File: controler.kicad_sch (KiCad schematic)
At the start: 37 parts, among them J1 USB_BOOT, J12 Conn_01x04_Pin, J2 Conn_ARM_JTAG_SWD_10, SW1 SW_DIP_x08, U1 NCP1117-3.3_SOT223, U1 RP2040, U2 W25Q128JVS, Y1 Crystal

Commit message: ECR fixes
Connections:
- net SWCLK is gone; now on net SWDCLK: U1.24 (SWCLK)
- net GND: no longer U1.28 (GPIO17)
- no-connect marks 2 -> 3
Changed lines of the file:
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@@
   (no_connect (at 185.42 138.43))
   (no_connect (at 185.42 135.89))
+  (no_connect (at 130.81 95.25))
   (wire (pts (xy 222.25 30.48) (xy 209.55 30.48))
     (stroke (width 0) (type default))
@@
     (stroke (width 0) (type default))
   )
-  (wire (pts (xy 144.78 95.25) (xy 130.81 95.25))
-    (stroke (width 0) (type default))
-  )
   (wire (pts (xy 102.87 44.45) (xy 102.87 41.91))
-    (stroke (width 0) (type default))
-  )
-  (wire (pts (xy 144.78 97.79) (xy 144.78 95.25))
     (stroke (width 0) (type default))
   )
@@
     (effects (font (size 1.27 1.27)) (justify left bottom))
   )
-  (label "SWCLK" (at 77.47 118.11 180) (fields_autoplaced)
+  (label "SWDCLK" (at 77.47 118.11 180) (fields_autoplaced)
     (effects (font (size 1.27 1.27)) (justify right bottom))
   )
@@
     (effects (font (size 1.27 1.27)) (justify left))
   )
-  (hierarchical_label "3V3" (shape output) (at 90.17 162.56 0) (fields_autoplaced)
+  (hierarchical_label "+3V3" (shape output) (at 90.17 162.56 0) (fields_autoplaced)
     (effects (font (size 1.27 1.27)) (justify left))
   )
@@
         )
       )
-    )
-  )
-  (symbol (lib_id "power:GND") (at 144.78 97.79 0) (unit 1)
-    (in_bom yes) (on_board yes) (dnp no) (fields_autoplaced)
-    (property "Reference" "#PWR049" (at 144.78 104.14 0)
-      (effects (font (size 1.27 1.27)) hide)
-    )
-    (property "Value" "GND" (at 144.78 102.87 0)
-      (effects (font (size 1.27 1.27)))
-    )
-    (property "Footprint" "" (at 144.78 97.79 0)
-      (effects (font (size 1.27 1.27)) hide)
-    )
-    (property "Datasheet" "" (at 144.78 97.79 0)
-      (effects (font (size 1.27 1.27)) hide)
-    )
-    (pin "1")
-    (instances
-      (project "SmartishFairy"
-        (path "/c494d399-9c3e-4fb0-8fd0-96c74769e433/c3e5f29d-a8aa-4f99-a65b-6663a6477720"
-          (reference "#PWR049") (unit 1)
-        )
-      )

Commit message: More ECR fixes
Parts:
- added R30: 1K, symbol Device:R
- R24, R25, R26, R27: value R -> 1K
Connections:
- net GND: now also R30.2
- net at U1.28 (GPIO17): now also R30.1
- no-connect marks 3 -> 2
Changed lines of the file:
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@@
   (no_connect (at 185.42 138.43))
   (no_connect (at 185.42 135.89))
-  (no_connect (at 130.81 95.25))
   (wire (pts (xy 222.25 30.48) (xy 209.55 30.48))
     (stroke (width 0) (type default))
@@
     (stroke (width 0) (type default))
   )
+  (wire (pts (xy 130.81 95.25) (xy 139.7 95.25))
+    (stroke (width 0) (type default))
+  )
   (wire (pts (xy 130.81 62.23) (xy 133.35 62.23))
     (stroke (width 0) (type default))
@@
     (stroke (width 0) (type default))
   )
+  (wire (pts (xy 156.21 97.79) (xy 156.21 95.25))
+    (stroke (width 0) (type default))
+  )
   (wire (pts (xy 34.29 162.56) (xy 49.53 162.56))
     (stroke (width 0) (type default))
@@
   )
   (wire (pts (xy 62.23 97.79) (xy 62.23 99.06))
+    (stroke (width 0) (type default))
+  )
+  (wire (pts (xy 147.32 95.25) (xy 156.21 95.25))
     (stroke (width 0) (type default))
   )
@@
     )
   )
+  (symbol (lib_id "Device:R") (at 143.51 95.25 90) (unit 1)
+    (in_bom yes) (on_board yes) (dnp no) (fields_autoplaced)
+    (property "Reference" "R30" (at 143.51 90.17 90)
+      (effects (font (size 1.27 1.27)))
+    )
+    (property "Value" "1K" (at 143.51 92.71 90)
+      (effects (font (size 1.27 1.27)))
+    )
+    (property "Footprint" "" (at 143.51 97.028 90)
+      (effects (font (size 1.27 1.27)) hide)
+    )
+    (property "Datasheet" "~" (at 143.51 95.25 0)
+      (effects (font (size 1.27 1.27)) hide)
+    )
+    (pin "1")
+    (pin "2")
+    (instances
+      (project "SmartishFairy"
+        (path "/c494d399-9c3e-4fb0-8fd0-96c74769e433/c3e5f29d-a8aa-4f99-a65b-6663a6477720"
+          (reference "R30") (unit 1)
+        )
+      )
+    )
+  )
   (symbol (lib_id "power:GND") (at 172.72 153.67 0) (unit 1)
     (in_bom yes) (on_board yes) (dnp no)
@@
       (effects (font (size 1.27 1.27)) (justify left))
     )
-    (property "Value" "R" (at 179.07 75.565 0)
+    (property "Value" "1K" (at 179.07 75.565 0)
       (effects (font (size 1.27 1.27)) (justify left))
     )
@@
         (path "/c494d399-9c3e-4fb0-8fd0-96c74769e433/c3e5f29d-a8aa-4f99-a65b-6663a6477720"
           (reference "#PWR070") (unit 1)
+        )
+      )
+    )
+  )
+  (symbol (lib_id "power:GND") (at 156.21 97.79 0) (unit 1)
+    (in_bom yes) (on_board yes) (dnp no) (fields_autoplaced)
+    (property "Reference" "#PWR049" (at 156.21 104.14 0)
+      (effects (font (size 1.27 1.27)) hide)
+    )
+    (property "Value" "GND" (at 156.21 102.87 0)
+      (effects (font (size 1.27 1.27)))
+    )
+    (property "Footprint" "" (at 156.21 97.79 0)
+      (effects (font (size 1.27 1.27)) hide)
+    )
+    (property "Datasheet" "" (at 156.21 97.79 0)
+      (effects (font (size 1.27 1.27)) hide)
+    )
+    (pin "1")
+    (instances
+      (project "SmartishFairy"
+        (path "/c494d399-9c3e-4fb0-8fd0-96c74769e433/c3e5f29d-a8aa-4f99-a65b-6663a6477720"
+          (reference "#PWR049") (unit 1)
         )
       )
@@
       (effects (font (size 1.27 1.27)) (justify left))
     )
-    (property "Value" "R" (at 199.39 75.565 0)
+    (property "Value" "1K" (at 199.39 75.565 0)
       (effects (font (size 1.27 1.27)) (justify left))
     )
@@
       (effects (font (size 1.27 1.27)) (justify left))
     )
-    (property "Value" "R" (at 189.23 75.565 0)
+    (property "Value" "1K" (at 189.23 75.565 0)
       (effects (font (size 1.27 1.27)) (justify left))
     )
@@
       (effects (font (size 1.27 1.27)) (justify left))
     )
-    (property "Value" "R" (at 209.55 75.565 0)
-      (effects (font (size 1.27 1.27)) (justify left))
-    )
+    (property "Value" "1K" (at 209.55 75.565 0)
+      (effects (font (size 1.27 1.27)) (justify left))
+    )

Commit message: ECR fixes
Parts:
- C1, C4: value 10u -> 10uF
- C19, C20, C21, C22, C23, C24, C25, C26, C27, C28, C29, C30, C31, C32: footprint (none) -> Capacitor_SMD:C_0805_2012Metric
- D4, D5, D6, D7: footprint (none) -> LED_SMD:LED_0805_2012Metric
- J1: footprint (none) -> Connector_PinHeader_2.54mm:PinHeader_1x02_P2.54mm_Vertical
- J12: footprint (none) -> Connector_PinHeader_2.54mm:PinHeader_1x04_P2.54mm_Vertical
- J2: footprint (none) -> Connector_PinHeader_1.27mm:PinHeader_2x05_P1.27mm_Vertical_SMD
- R19, R20, R21, R22, R23, R24, R25, R26, R27, R30: footprint (none) -> Resistor_SMD:R_0805_2012Metric
- SW1: footprint (none) -> Button_Switch_THT:SW_DIP_SPSTx08_Slide_9.78x22.5mm_W7.62mm_P2.54mm
- Y1: footprint (none) -> Crystal:Crystal_SMD_HC49-SD
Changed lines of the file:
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@@
       (effects (font (size 1.27 1.27)) (justify left))
     )
-    (property "Footprint" "" (at 196.85 83.82 0)
+    (property "Footprint" "LED_SMD:LED_0805_2012Metric" (at 196.85 83.82 0)
       (effects (font (size 1.27 1.27)) hide)
     )
@@
       (effects (font (size 1.27 1.27)) (justify left))
     )
-    (property "Footprint" "" (at 159.7152 40.64 0)
+    (property "Footprint" "Capacitor_SMD:C_0805_2012Metric" (at 159.7152 40.64 0)
       (effects (font (size 1.27 1.27)) hide)
     )
@@
       (effects (font (size 1.27 1.27)) (justify left))
     )
-    (property "Footprint" "" (at 147.0152 40.64 0)
+    (property "Footprint" "Capacitor_SMD:C_0805_2012Metric" (at 147.0152 40.64 0)
       (effects (font (size 1.27 1.27)) hide)
     )
@@
       (effects (font (size 1.27 1.27)) (justify left))
     )
-    (property "Footprint" "" (at 223.2152 40.64 0)
+    (property "Footprint" "Capacitor_SMD:C_0805_2012Metric" (at 223.2152 40.64 0)
       (effects (font (size 1.27 1.27)) hide)
     )
@@
       (effects (font (size 1.27 1.27)))
     )
-    (property "Footprint" "" (at 143.51 97.028 90)
+    (property "Footprint" "Resistor_SMD:R_0805_2012Metric" (at 143.51 97.028 90)
       (effects (font (size 1.27 1.27)) hide)
     )
@@
       (effects (font (size 1.27 1.27)))
     )
-    (property "Footprint" "" (at 73.66 60.452 90)
+    (property "Footprint" "Resistor_SMD:R_0805_2012Metric" (at 73.66 60.452 90)
       (effects (font (size 1.27 1.27)) hide)
     )
@@
       (effects (font (size 1.27 1.27)))
     )
-    (property "Footprint" "" (at 48.26 106.9848 0)
+    (property "Footprint" "Capacitor_SMD:C_0805_2012Metric" (at 48.26 106.9848 0)
       (effects (font (size 1.27 1.27)) hide)
     )
@@
       (effects (font (size 1.27 1.27)))
     )
-    (property "Footprint" "" (at 72.39 106.172 90)
+    (property "Footprint" "Resistor_SMD:R_0805_2012Metric" (at 72.39 106.172 90)
       (effects (font (size 1.27 1.27)) hide)
     )
@@
       (effects (font (size 1.27 1.27)) (justify left))
     )
-    (property "Footprint" "" (at 207.01 83.82 0)
+    (property "Footprint" "LED_SMD:LED_0805_2012Metric" (at 207.01 83.82 0)
       (effects (font (size 1.27 1.27)) hide)
     )
@@
       (effects (font (size 1.27 1.27)) (justify left))
     )
-    (property "Footprint" "" (at 185.1152 40.64 0)
+    (property "Footprint" "Capacitor_SMD:C_0805_2012Metric" (at 185.1152 40.64 0)
       (effects (font (size 1.27 1.27)) hide)
     )
@@
       (effects (font (size 1.27 1.27)) (justify left))
     )
-    (property "Footprint" "" (at 174.752 73.66 90)
+    (property "Footprint" "Resistor_SMD:R_0805_2012Metric" (at 174.752 73.66 90)
       (effects (font (size 1.27 1.27)) hide)
     )
@@
       (effects (font (size 1.27 1.27)))
     )
-    (property "Footprint" "" (at 250.19 77.47 0)
+    (property "Footprint" "Button_Switch_THT:SW_DIP_SPSTx08_Slide_9.78x22.5mm_W7.62mm_P2.54mm" (at 250.19 77.47 0)
       (effects (font (size 1.27 1.27)) hide)
     )
@@
       (effects (font (size 1.27 1.27)) (justify left))
     )
-    (property "Footprint" "" (at 59.3852 40.64 0)
+    (property "Footprint" "Capacitor_SMD:C_0805_2012Metric" (at 59.3852 40.64 0)
       (effects (font (size 1.27 1.27)) hide)
     )
@@
       (effects (font (size 1.27 1.27)) (justify right))
     )
-    (property "Footprint" "" (at 172.72 133.35 0)
+    (property "Footprint" "Connector_PinHeader_1.27mm:PinHeader_2x05_P1.27mm_Vertical_SMD" (at 172.72 133.35 0)
       (effects (font (size 1.27 1.27)) hide)
     )
@@
       (effects (font (size 1.27 1.27)) (justify right))
     )
-    (property "Footprint" "" (at 263.398 127 90)
+    (property "Footprint" "Resistor_SMD:R_0805_2012Metric" (at 263.398 127 90)
       (effects (font (size 1.27 1.27)) hide)
     )
@@
       (effects (font (size 1.27 1.27)) (justify left))
     )
-    (property "Footprint" "" (at 210.5152 40.64 0)
+    (property "Footprint" "Capacitor_SMD:C_0805_2012Metric" (at 210.5152 40.64 0)
       (effects (font (size 1.27 1.27)) hide)
     )
@@
       (effects (font (size 1.27 1.27)) (justify right))
     )
-    (property "Footprint" "" (at 62.23 102.87 0)
+    (property "Footprint" "Crystal:Crystal_SMD_HC49-SD" (at 62.23 102.87 0)
       (effects (font (size 1.27 1.27)) hide)
     )
@@
       (effects (font (size 1.27 1.27)))
     )
-    (property "Footprint" "" (at 73.66 53.848 90)
+    (property "Footprint" "Resistor_SMD:R_0805_2012Metric" (at 73.66 53.848 90)
       (effects (font (size 1.27 1.27)) hide)
     )
@@
       (effects (font (size 1.27 1.27)) (justify right))
     )
-    (property "Footprint" "" (at 266.7 142.24 0)
+    (property "Footprint" "Connector_PinHeader_2.54mm:PinHeader_1x02_P2.54mm_Vertical" (at 266.7 142.24 0)
       (effects (font (size 1.27 1.27)) hide)
     )
@@
       (effects (font (size 1.27 1.27)) (justify left))
     )
-    (property "Footprint" "" (at 172.4152 40.64 0)
+    (property "Footprint" "Capacitor_SMD:C_0805_2012Metric" (at 172.4152 40.64 0)
       (effects (font (size 1.27 1.27)) hide)
     )
@@
       (effects (font (size 1.27 1.27)) (justify left))
     )
-    (property "Footprint" "" (at 197.8152 40.64 0)
+    (property "Footprint" "Capacitor_SMD:C_0805_2012Metric" (at 197.8152 40.64 0)
       (effects (font (size 1.27 1.27)) hide)
     )
@@
       (effects (font (size 1.27 1.27)) (justify left))
     )
-    (property "Footprint" "" (at 221.9452 120.65 0)
+    (property "Footprint" "Capacitor_SMD:C_0805_2012Metric" (at 221.9452 120.65 0)
       (effects (font (size 1.27 1.27)) hide)
     )
@@
       (effects (font (size 1.27 1.27)) (justify left))
     )
-    (property "Footprint" "" (at 176.53 83.82 0)
+    (property "Footprint" "LED_SMD:LED_0805_2012Metric" (at 176.53 83.82 0)
       (effects (font (size 1.27 1.27)) hide)
     )
@@
       (effects (font (size 1.27 1.27)) (justify left))
     )
-    (property "Footprint" "" (at 195.072 73.66 90)
+    (property "Footprint" "Resistor_SMD:R_0805_2012Metric" (at 195.072 73.66 90)
       (effects (font (size 1.27 1.27)) hide)
     )
@@
       (effects (font (size 1.27 1.27)))
     )
-    (property "Footprint" "" (at 55.88 96.8248 0)
+    (property "Footprint" "Capacitor_SMD:C_0805_2012Metric" (at 55.88 96.8248 0)
       (effects (font (size 1.27 1.27)) hide)
     )
@@
       (effects (font (size 1.27 1.27)) (justify left))
     )
-    (property "Footprint" "" (at 93.0148 40.64 0)
+    (property "Footprint" "Capacitor_SMD:C_0805_2012Metric" (at 93.0148 40.64 0)
       (effects (font (size 1.27 1.27)) hide)
     )
@@
       (effects (font (size 1.27 1.27)) (justify left))
     )
-    (property "Footprint" "" (at 46.6852 40.64 0)
+    (property "Footprint" "Capacitor_SMD:C_0805_2012Metric" (at 46.6852 40.64 0)
       (effects (font (size 1.27 1.27)) hide)
     )
@@
       (effects (font (size 1.27 1.27)) (justify left))
     )
-    (property "Value" "10u" (at 52.451 168.783 0)
+    (property "Value" "10uF" (at 52.451 168.783 0)
       (effects (font (size 1.27 1.27)) (justify left))
     )
@@
       (effects (font (size 1.27 1.27)))
     )
-    (property "Footprint" "" (at 73.66 61.468 90)
+    (property "Footprint" "Resistor_SMD:R_0805_2012Metric" (at 73.66 61.468 90)
       (effects (font (size 1.27 1.27)) hide)
     )
@@
       (effects (font (size 1.27 1.27)) (justify left))
     )
-    (property "Footprint" "" (at 186.69 83.82 0)
+    (property "Footprint" "LED_SMD:LED_0805_2012Metric" (at 186.69 83.82 0)
       (effects (font (size 1.27 1.27)) hide)
     )
@@
       (effects (font (size 1.27 1.27)) (justify left))
     )
-    (property "Footprint" "" (at 184.912 73.66 90)
+    (property "Footprint" "Resistor_SMD:R_0805_2012Metric" (at 184.912 73.66 90)
       (effects (font (size 1.27 1.27)) hide)
     )
@@
       (effects (font (size 1.27 1.27)) (justify left))
     )
-    (property "Footprint" "" (at 205.232 73.66 90)
+    (property "Footprint" "Resistor_SMD:R_0805_2012Metric" (at 205.232 73.66 90)
       (effects (font (size 1.27 1.27)) hide)
     )
@@
       (effects (font (size 1.27 1.27)) (justify left))
     )
-    (property "Value" "10u" (at 88.011 168.783 0)
+    (property "Value" "10uF" (at 88.011 168.783 0)
       (effects (font (size 1.27 1.27)) (justify left))
     )
@@
       (effects (font (size 1.27 1.27)))
     )
-    (property "Footprint" "" (at 121.92 166.37 0)
+    (property "Footprint" "Connector_PinHeader_2.54mm:PinHeader_1x04_P2.54mm_Vertical" (at 121.92 166.37 0)
       (effects (font (size 1.27 1.27)) hide)
     )
@@
       (effects (font (size 1.27 1.27)) (justify left))
     )
-    (property "Footprint" "" (at 121.6152 40.64 0)
-      (effects (font (size 1.27 1.27)) hide)
-    )
+    (property "Footprint" "Capacitor_SMD:C_0805_2012Metric" (at 121.6152 40.64 0)
+      (effects (font (size 1.27 1.27)) hide)
+    )

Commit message: Layout WIP
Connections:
- net GND: now also D4.1 (K), D5.1 (K), D6.1 (K), D7.1 (K); no longer D4.2 (A), D5.2 (A), D6.2 (A), D7.2 (A)
- net at R26.2: now also D6.2 (A); no longer D6.1 (K)
- net at R27.2: now also D7.2 (A); no longer D7.1 (K)
- net at R24.2: now also D4.2 (A); no longer D4.1 (K)
- net at R25.2: now also D5.2 (A); no longer D5.1 (K)
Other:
- moved on the sheet: D4, D5, D6, D7

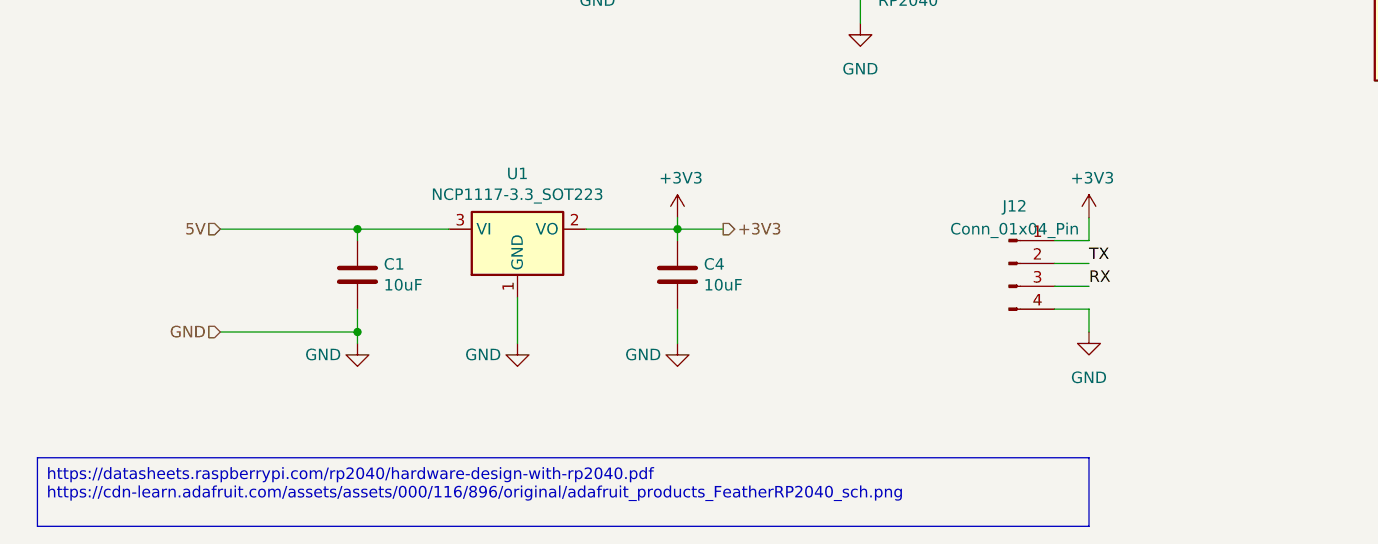
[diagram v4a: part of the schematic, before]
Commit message: Convert to KiCAD v9 and basic sort out of components
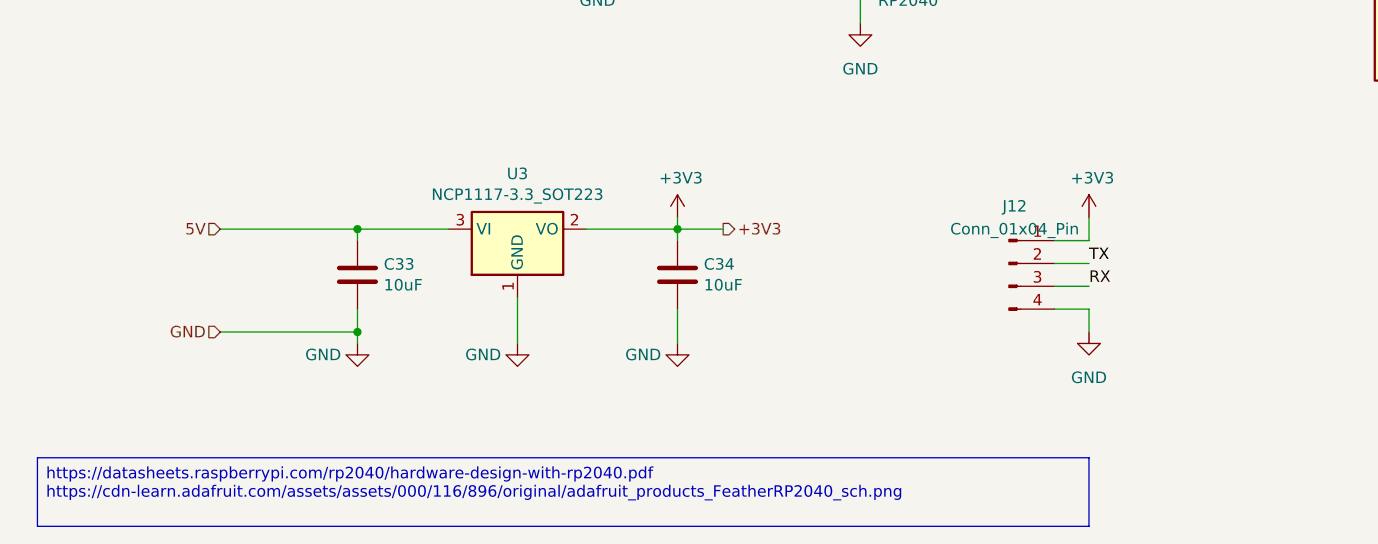
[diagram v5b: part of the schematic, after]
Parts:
- renumbered C1 to C33, C4 to C34, U1 to U3

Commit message: Additional layout
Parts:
- removed Y1: Crystal, Crystal:Crystal_SMD_HC49-SD, symbol Device:Crystal
- added Y1: 12MHz, Crystal:Crystal_SMD_3225-4Pin_3.2x2.5mm, symbol Device:Crystal_GND24
- C19, C20, C21, C22, C23, C24, C25, C26, C27, C28, C29, C30, C31, C32, C33, C34: footprint Capacitor_SMD:C_0805_2012Metric -> Capacitor_SMD:C_0603_1608Metric
- R19, R20, R21, R22, R23, R24, R25, R26, R27, R30: footprint Resistor_SMD:R_0805_2012Metric -> Resistor_SMD:R_0603_1608Metric
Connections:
- net GND: now also Y1.2, Y1.4
- net at C31.1, R22.2: now also Y1.3
- net at C30.2, U1.20 (XIN): now also Y1.1
